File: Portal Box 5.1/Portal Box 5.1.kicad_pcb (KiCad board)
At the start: 2 copper layers, 120 x 80 mm, 79 parts, among them J1 USB_A, J2 USB_C, J3 A 14-LC-TT, J4 6871XX149022_687118149022, J5 RFID-RC522, J6 Conn_01x04, K1 PR28-5V-360-1A-E, Q1 NTR5103NT1G, Q2 NTR5103NT1G, SW1 BUTTON, SW2 SW_DPST, U1 USBLC6-2P6, U2 USBLC6-2P6, U3 TLE4971-A050T5-U-E0001, U4 AP7363-33D-13, U5 ESP32-S3-DEVKITC-1-N8R8-OFFIC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

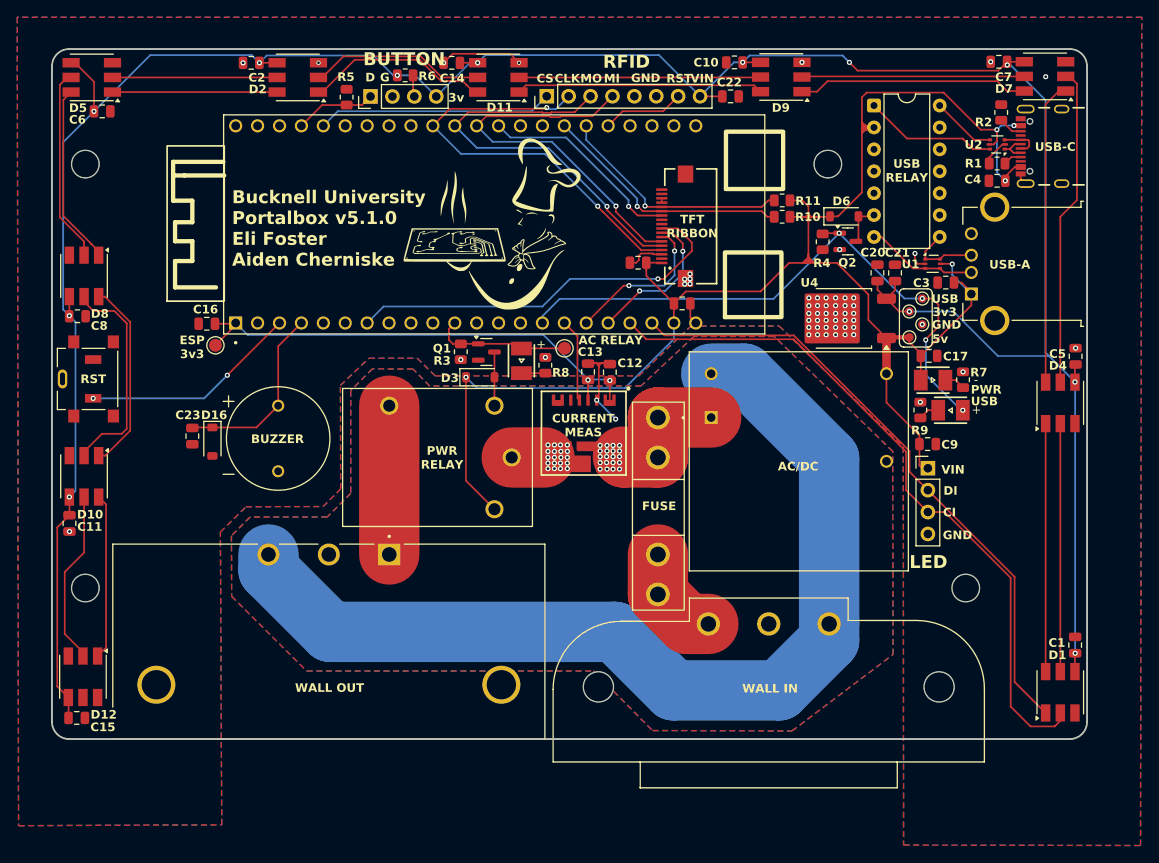
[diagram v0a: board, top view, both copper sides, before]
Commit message: update track clearances, mfg files
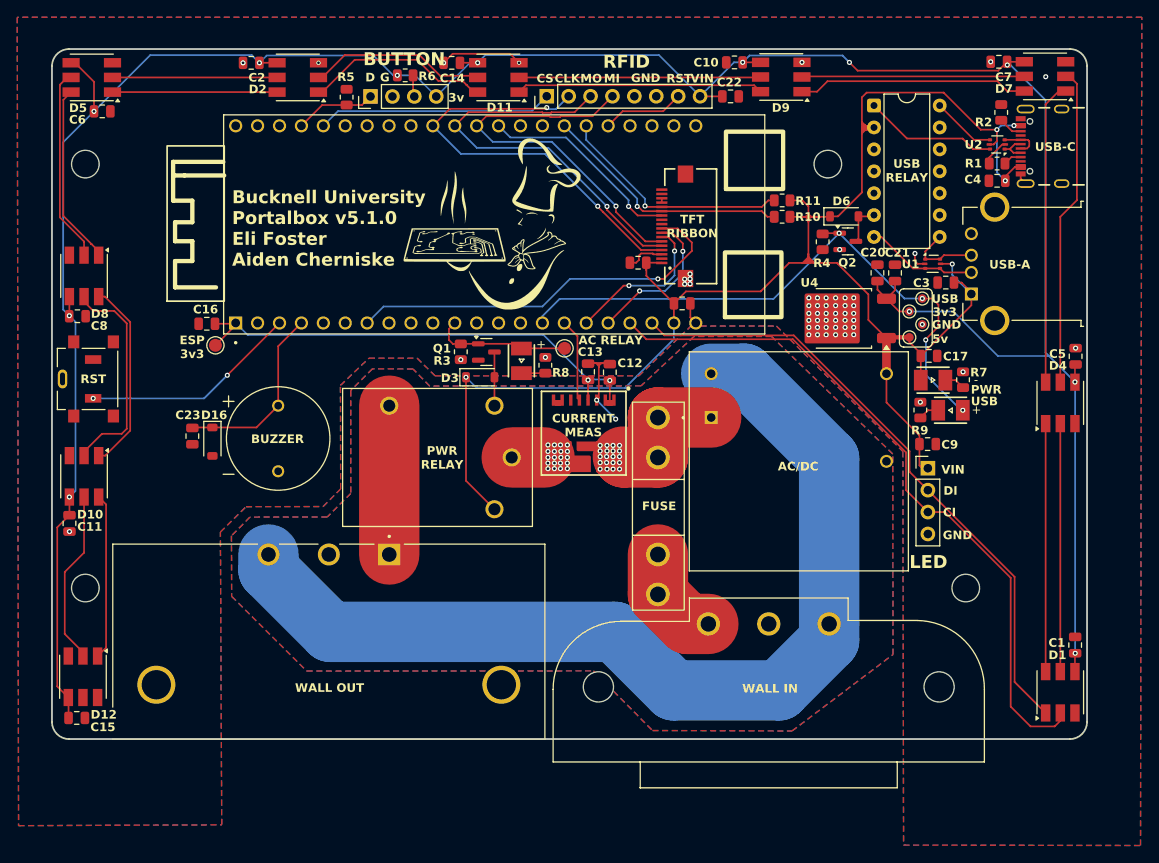
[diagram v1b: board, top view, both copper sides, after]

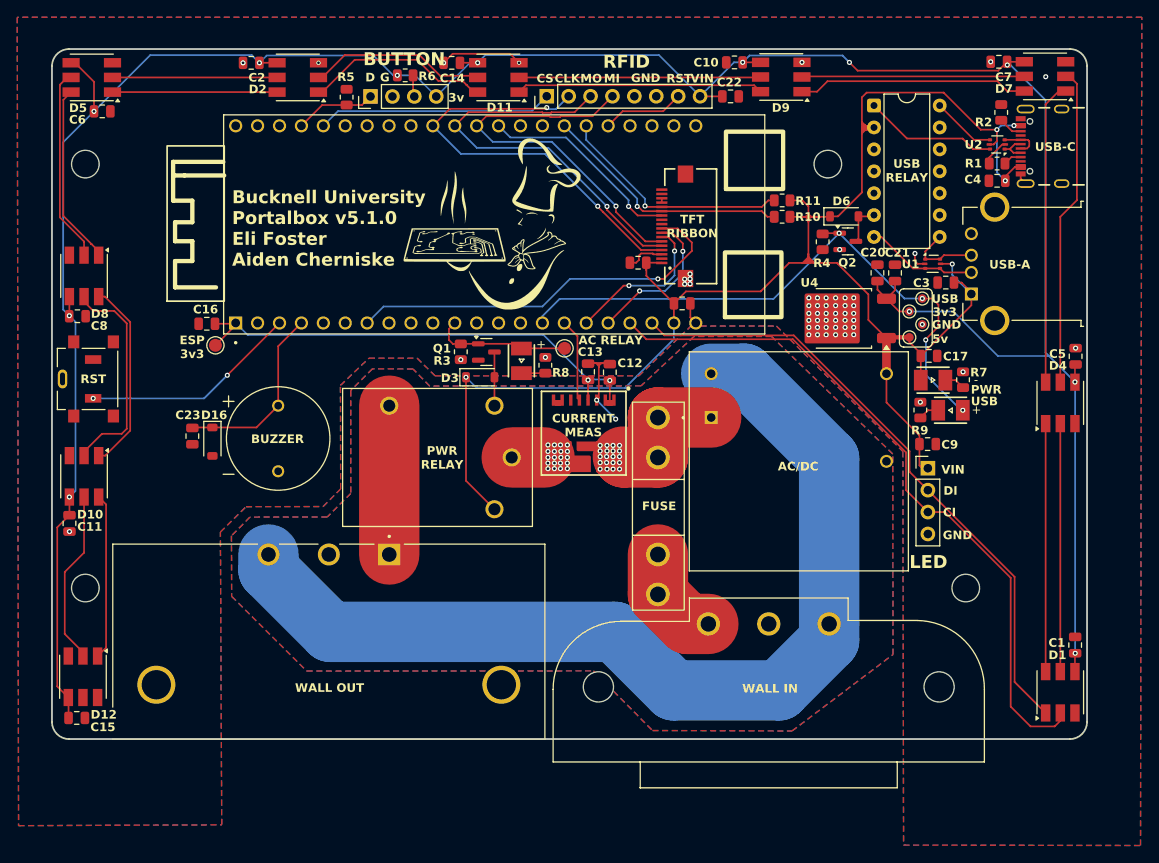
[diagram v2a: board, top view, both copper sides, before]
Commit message: change ac/dc and acm to dc ground, update planes
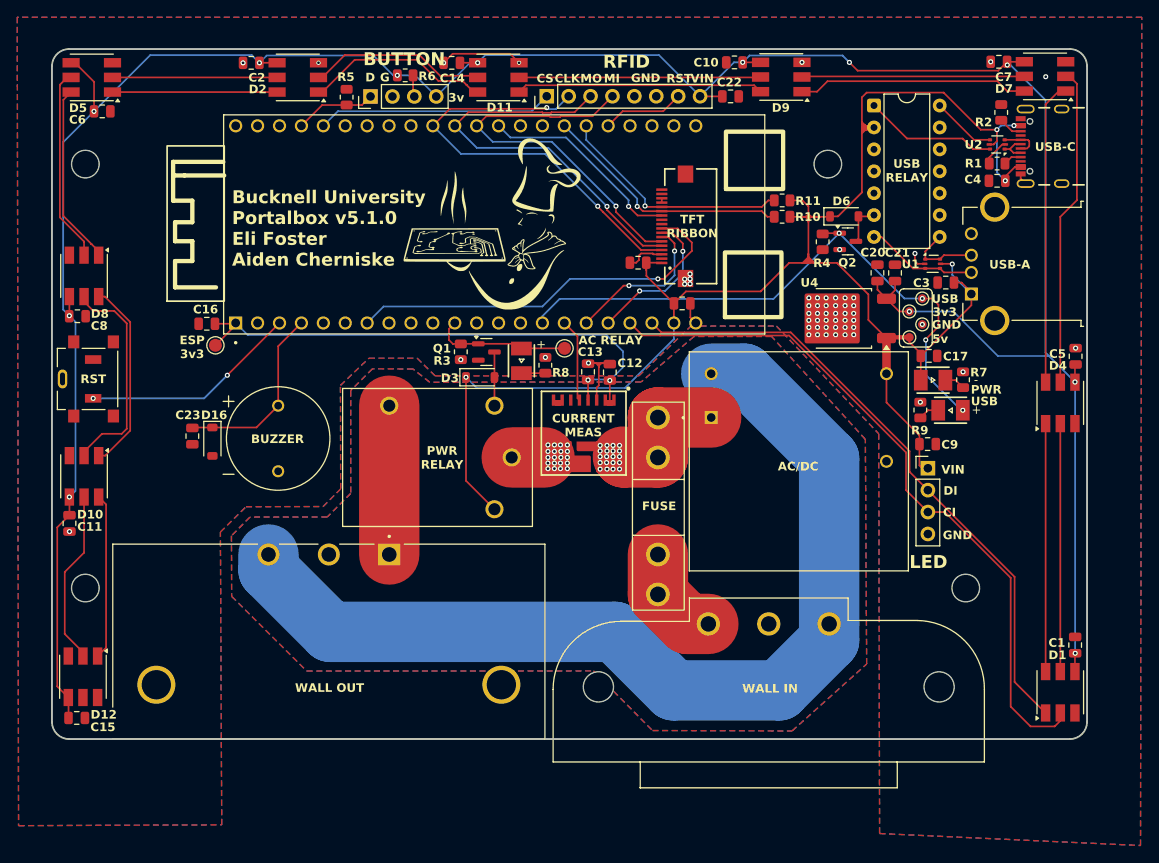
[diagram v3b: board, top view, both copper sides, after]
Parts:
- A1: value 703W-00_53 -> Q219-ND
- A2: value PX0675/PC -> 708-1351-ND
- BZ1: value Buzzer -> 668-AI-1223-TWT-5V-7-ND
- J1: value USB_A -> 609-87520-0010ALFCT-ND
- J2: value USB_C -> 2073-USB4105-GF-ACT-ND
- J4: value 6871XX149022_687118149022 -> 732-6001-1-ND
- PS1: value RACM06E-05SK_277 -> 945-RACM06E-05SK/277-ND
- SW1: value BUTTON -> 141-TL3336AF160QCT-ND
- U1, U2: value USBLC6-2P6 -> 497-5026-1-ND
- U3: value TLE4971-A050T5-U-E0001 -> 448-TLE4971A050T5UE0001XUMA1CT-ND
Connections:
- C12 pad 2: Earth -> GND
- C13 pad 2: Earth -> GND
- PS1 pad 4: Earth -> GND
- U3 pad 2: Earth -> GND
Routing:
- net Earth: track 12.5 -> 0.00 mm, vias 2 -> 0
- net GND: track 23.8 -> 33.2 mm, vias 57 -> 58
- net ESP3vo: track 58.0 -> 64.7 mm

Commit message: fix ground plane bulges, schematic and layout change for TVS diodes
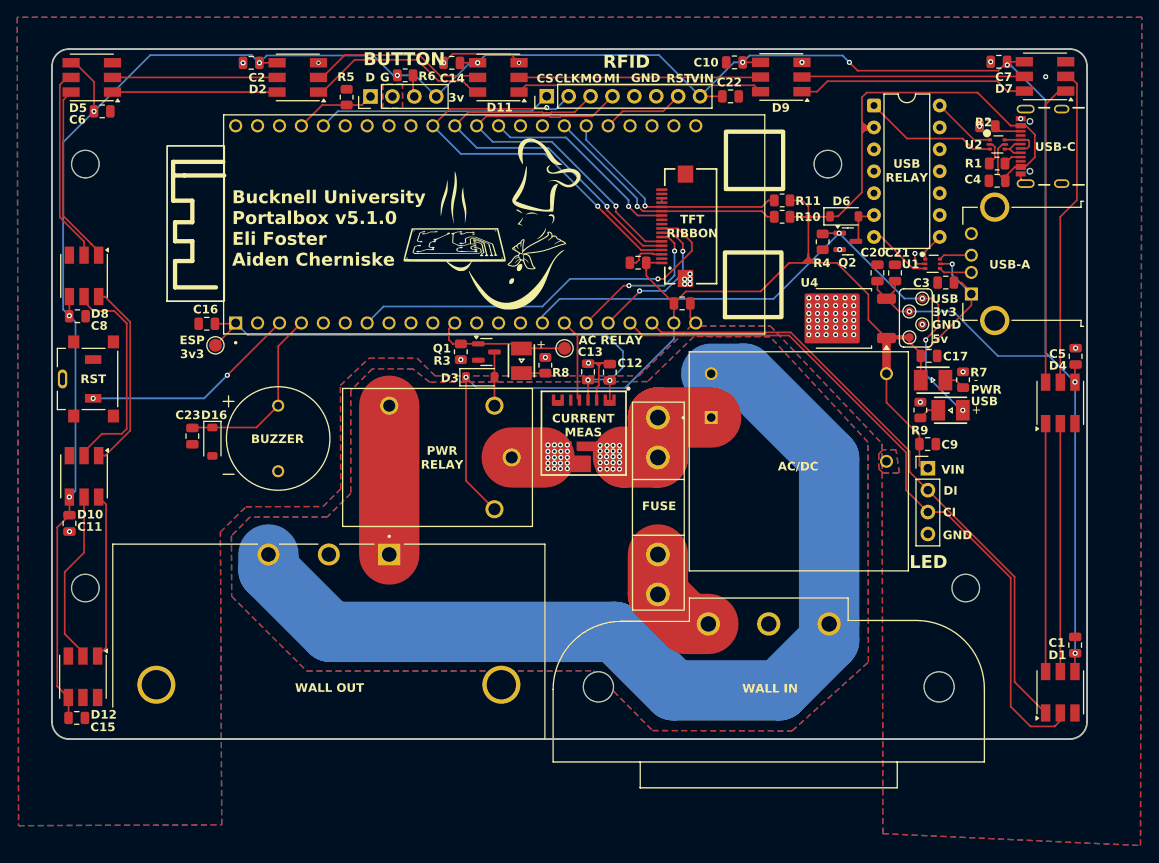
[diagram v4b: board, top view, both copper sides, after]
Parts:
- moved R2 2.26 mm to (197.4, 62.1), turned to 0 degrees
- turned U2 to 0 degrees
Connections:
- J1 pad 2: USBA_D- -> /A_D-
- J1 pad 3: USBA_D+ -> /A_D+
- U1 pad 4: USBA_D- -> /A_D-
- U1 pad 6: USBA_D+ -> /A_D+
- U2 pad 1: /C_D- -> USBC_D+
- U2 pad 3: /C_D+ -> USBC_D-
- U2 pad 4: USBC_D+ -> /C_D-
- U2 pad 6: USBC_D- -> /C_D+
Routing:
- net USBA_D+: track 8.84 -> 3.26 mm
- net USBA_D-: track 13.0 -> 7.46 mm
- net /A_D+: track 0.00 -> 3.87 mm
- net /A_D-: track 0.00 -> 3.83 mm
- net +5V: track 209.8 -> 212.7 mm, vias 5 -> 2
- net GND: track 33.2 -> 33.0 mm, vias 58 -> 60

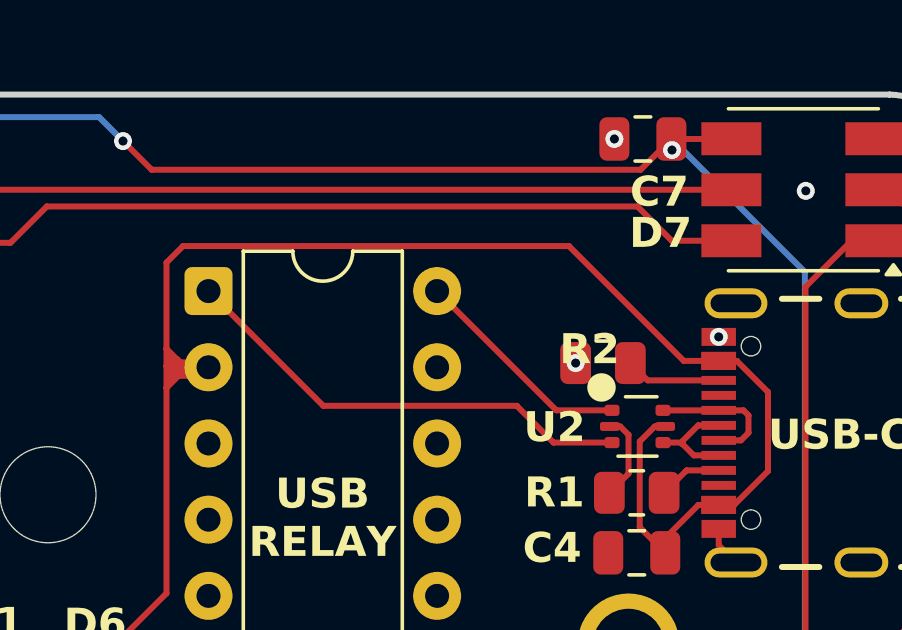
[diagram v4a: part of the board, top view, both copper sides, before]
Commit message: move r2 and fix silkscreening, update tvs diode footprint
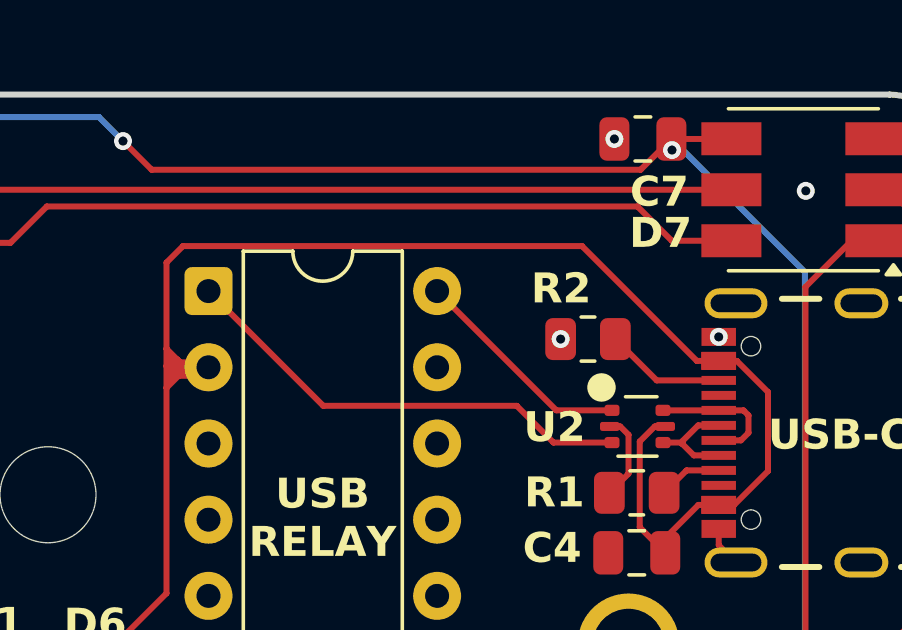
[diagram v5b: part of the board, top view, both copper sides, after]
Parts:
- moved R2 0.94 mm to (196.9, 61.3)
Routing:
- net /CC2: track 3.18 -> 4.02 mm
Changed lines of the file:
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@@
 	(footprint "Resistor_SMD:R_0805_2012Metric"
 		(layer "F.Cu")
-		(at 197.4 62.1)
+		(at 196.9 61.3)
 		(descr "Resistor SMD 0805 (2012 Metric), square (rectangular) end terminal, IPC-7351 nominal, (Body size source: IPC-SM-782 page 72, https://www.pcb-3d.com/wordpress/wp-content/uploads/ipc-sm-782a_amendment_1_and_2.pdf), generated with kicad-footprint-generator")
 		(tags "resistor")
@@
 	)
 	(gr_text "R2"
-		(at 195.95 62.225 0)
+		(at 195 60.2 0)
 		(layer "F.SilkS")
 		(effects
@@
 	)
 	(via
-		(at 196.4875 62.1)
+		(at 195.9875 61.3)
 		(size 0.6)
 		(drill 0.3)
@@
 	)
 	(segment
-		(start 196.265 58.2)
-		(end 183.4 58.2)
+		(start 200.5275 62.0275)
+		(end 196.7 58.2)
 		(width 0.2)
 		(layer "F.Cu")
@@
 	)
 	(segment
+		(start 182.85 58.75)
+		(end 182.85 61.625)
+		(width 0.2)
+		(layer "F.Cu")
+		(net 6)
+	)
+	(segment
 		(start 176.325 77.95)
 		(end 176.175 77.95)
@@
 	)
 	(segment
+		(start 183.4 58.2)
+		(end 182.85 58.75)
+		(width 0.2)
+		(layer "F.Cu")
+		(net 6)
+	)
+	(segment
 		(start 183.2 61.975)
 		(end 183.3 62.075)
@@
 	)
 	(segment
-		(start 183.4 58.2)
-		(end 182.85 58.75)
-		(width 0.2)
-		(layer "F.Cu")
-		(net 6)
-	)
-	(segment
 		(start 183.2 61.975)
 		(end 182.85 61.625)
@@
 	)
 	(segment
+		(start 201.2625 62.0275)
+		(end 200.5275 62.0275)
+		(width 0.2)
+		(layer "F.Cu")
+		(net 6)
+	)
+	(segment
 		(start 183.25 62.525)
 		(end 182.85 62.925)
@@
 	)
 	(segment
-		(start 201.2625 62.0275)
-		(end 200.0925 62.0275)
-		(width 0.2)
-		(layer "F.Cu")
-		(net 6)
-	)
-	(segment
 		(start 183.3 62.075)
 		(end 183.6 62.075)
@@
 	)
 	(segment
-		(start 182.85 58.75)
-		(end 182.85 61.625)
-		(width 0.2)
-		(layer "F.Cu")
-		(net 6)
-	)
-	(segment
 		(start 176.175 77.95)
 		(end 176.675 77.45)
@@
 	)
 	(segment
-		(start 200.0925 62.0275)
-		(end 196.265 58.2)
-		(width 0.2)
-		(layer "F.Cu")
-		(net 6)
-	)
-	(segment
 		(start 176.649 76.925)
 		(end 176.649 73.175)
@@
 	)
 	(segment
+		(start 196.7 58.2)
+		(end 183.4 58.2)
+		(width 0.2)
+		(layer "F.Cu")
+		(net 6)
+	)
+	(segment
 		(start 176.649 73.175)
 		(end 176.649 72.926)
@@
 	)
 	(segment
-		(start 198.89 62.6775)
-		(end 201.2575 62.6775)
+		(start 201.2575 62.6775)
+		(end 199.19 62.6775)
 		(width 0.2)
 		(layer "F.Cu")
@@
 	)
 	(segment
-		(start 198.3125 62.1)
-		(end 198.89 62.6775)
+		(start 199.19 62.6775)
+		(end 197.8125 61.3)
 		(width 0.2)
 		(layer "F.Cu")
@@
 	)
 	(zone
+		(net 6)
+		(net_name "+5V")
+		(layer "F.Cu")
+		(name "$teardrop_padvia$")
+		(hatch full 0.1)
+		(priority 30003)
+		(attr
+			(teardrop
+				(type padvia)
+			)
+		)
+		(connect_pads yes
+			(clearance 0)
+		)
+		(min_thickness 0.0254)
+		(filled_areas_thickness no)
+		(fill yes
+			(thermal_gap 0.5)
+			(thermal_bridge_width 0.5)
+			(island_removal_mode 1)
+			(island_area_min 10)
+		)
+		(polygon
+			(pts
+				(xy 185.1975 87.86) (xy 186.1975 87.86) (xy 186.298751 87.26) (xy 185.7 86.659) (xy 185.098747 87.26)
+			)
+		)
+	)
+	(zone
 		(net 0)
 		(net_name "")
@@
 	)
 	(zone
-		(net 4)
-		(net_name "+3V3")
+		(net 6)
+		(net_name "+5V")
 		(layer "F.Cu")
 		(name "$teardrop_padvia$")
 		(hatch full 0.1)
-		(priority 30004)
+		(priority 30006)
 		(attr
 			(teardrop
@@
 		(polygon
 			(pts
-				(xy 184.746447 81.005026) (xy 184.605026 81.146447) (xy 184.6 81.75) (xy 185.700707 82.100707) (xy 185.948528 81.5)
+				(xy 184.746447 85.565026) (xy 184.605026 85.706447) (xy 184.6 86.31) (xy 185.700707 86.660707) (xy 185.948528 86.06)
 			)
 		)
 	)
 	(zone
-		(net 6)
-		(net_name "+5V")
+		(net 4)
+		(net_name "+3V3")
 		(layer "F.Cu")
 		(name "$teardrop_padvia$")
 		(hatch full 0.1)
-		(priority 30003)
+		(priority 30005)
 		(attr
 			(teardrop
@@
 		(polygon
 			(pts
-				(xy 185.1975 87.86) (xy 186.1975 87.86) (xy 186.298751 87.26) (xy 185.7 86.659) (xy 185.098747 87.26)
+				(xy 186.653553 83.194974) (xy 186.794974 83.053553) (xy 186.8 82.45) (xy 185.699293 82.099293) (xy 185.451472 82.7)
 			)
 		)
@@
 		(name "$teardrop_padvia$")
 		(hatch full 0.1)
-		(priority 30008)
+		(priority 30009)
 		(attr
 			(teardrop
@@
 		(polygon
 			(pts
-				(xy 187.755764 83.475) (xy 187.755764 83.675) (xy 188.291473 83.869236) (xy 188.351 83.575) (xy 188.291473 83.280764)
+				(xy 207.65 91.155764) (xy 207.45 91.155764) (xy 207.255764 91.691473) (xy 207.55 91.751) (xy 207.844236 91.691473)
 			)
 		)
@@
 		(name "$teardrop_padvia$")
 		(hatch full 0.1)
-		(priority 30006)
+		(priority 30001)
 		(attr
 			(teardrop
@@
 		(polygon
 			(pts
-				(xy 184.746447 85.565026) (xy 184.605026 85.706447) (xy 184.6 86.31) (xy 185.700707 86.660707) (xy 185.948528 86.06)
+				(xy 187.4 86.825) (xy 187.4 86.325) (xy 186.645671 86.07903) (xy 185.699 86.66) (xy 186.690198 87.211217)
 			)
 		)
 	)
 	(zone
-		(net 4)
-		(net_name "+3V3")
+		(net 6)
+		(net_name "+5V")
 		(layer "F.Cu")
 		(name "$teardrop_padvia$")
 		(hatch full 0.1)
-		(priority 30005)
+		(priority 30000)
 		(attr
 			(teardrop
@@
 		(polygon
 			(pts
-				(xy 186.653553 83.194974) (xy 186.794974 83.053553) (xy 186.8 82.45) (xy 185.699293 82.099293) (xy 185.451472 82.7)
+				(xy 186.1975 89.296488) (xy 185.1975 89.296488) (xy 184.957988 90.642902) (xy 185.6975 90.791) (xy 186.437012 90.642902)
 			)
 		)
 	)
 	(zone
-		(net 6)
-		(net_name "+5V")
+		(net 4)
+		(net_name "+3V3")
 		(layer "F.Cu")
 		(name "$teardrop_padvia$")
 		(hatch full 0.1)
-		(priority 30001)
+		(priority 30008)
 		(attr
 			(teardrop
@@
 		(polygon
 			(pts
-				(xy 187.4 86.825) (xy 187.4 86.325) (xy 186.645671 86.07903) (xy 185.699 86.66) (xy 186.690198 87.211217)
+				(xy 187.755764 83.475) (xy 187.755764 83.675) (xy 188.291473 83.869236) (xy 188.351 83.575) (xy 188.291473 83.280764)
 			)
 		)
@@
 		(name "$teardrop_padvia$")
 		(hatch full 0.1)
-		(priority 30009)
+		(priority 30007)
 		(attr
 			(teardrop
@@
 		(polygon
 			(pts
-				(xy 207.65 91.155764) (xy 207.45 91.155764) (xy 207.255764 91.691473) (xy 207.55 91.751) (xy 207.844236 91.691473)
+				(xy 186.79 81.061543) (xy 186.59 81.061543) (xy 185.443817 81.5) (xy 185.7 82.101) (xy 186.8 81.75)
 			)
 		)
 	)
 	(zone
-		(net 6)
-		(net_name "+5V")
+		(net 4)
+		(net_name "+3V3")
 		(layer "F.Cu")
 		(name "$teardrop_padvia$")
 		(hatch full 0.1)
-		(priority 30000)
+		(priority 30004)
 		(attr
 			(teardrop
@@
 		(polygon
 			(pts
-				(xy 186.1975 89.296488) (xy 185.1975 89.296488) (xy 184.957988 90.642902) (xy 185.6975 90.791) (xy 186.437012 90.642902)
+				(xy 184.746447 81.005026) (xy 184.605026 81.146447) (xy 184.6 81.75) (xy 185.700707 82.100707) (xy 185.948528 81.5)
 			)
 		)
@@
 	)
 	(zone
-		(net 4)
-		(net_name "+3V3")
-		(layer "F.Cu")
-		(name "$teardrop_padvia$")
-		(hatch full 0.1)
-		(priority 30007)
-		(attr
-			(teardrop
-				(type padvia)
-			)
-		)
-		(connect_pads yes
-			(clearance 0)
-		)
-		(min_thickness 0.0254)
-		(filled_areas_thickness no)
-		(fill yes
-			(thermal_gap 0.5)
-			(thermal_bridge_width 0.5)
-			(island_removal_mode 1)
-			(island_area_min 10)
-		)
-		(polygon
-			(pts
-				(xy 186.79 81.061543) (xy 186.59 81.061543) (xy 185.443817 81.5) (xy 185.7 82.101) (xy 186.8 81.75)
-			)
-		)
-	)
-	(zone
 		(net 5)
 		(net_name "GND")
@@
 		(name "$teardrop_padvia$")
 		(hatch full 0.1)
-		(priority 30001)
+		(priority 30000)
 		(attr
 			(teardrop
@@
 		(polygon
 			(pts
-				(xy 188.944236 83.675) (xy 188.944236 83.475) (xy 188.408527 83.280764) (xy 188.349 83.575) (xy 188.408527 83.869236)
+				(xy 207.475 92.344236) (xy 207.675 92.344236) (xy 207.844236 91.808527) (xy 207.55 91.749) (xy 207.255764 91.808527)
 			)
 		)
@@
 		(name "$teardrop_padvia$")
 		(hatch full 0.1)
-		(priority 30000)
+		(priority 30001)
 		(attr
 			(teardrop
@@
 		(polygon
 			(pts
-				(xy 207.475 92.344236) (xy 207.675 92.344236) (xy 207.844236 91.808527) (xy 207.55 91.749) (xy 207.255764 91.808527)
+				(xy 188.944236 83.675) (xy 188.944236 83.475) (xy 188.408527 83.280764) (xy 188.349 83.575) (xy 188.408527 83.869236)
 			)
 		)

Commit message: update revision number :)
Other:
- board text added: "Bucknell University Portalbox v5.1.1 Eli Foster Aiden Cherniske"
- board text removed: "Bucknell University Portalbox v5.1.0 Eli Foster Aiden Cherniske"
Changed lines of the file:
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@@
 		)
 	)
-	(gr_text "Bucknell University\nPortalbox v5.1.0\nEli Foster\nAiden Cherniske"
+	(gr_text "Bucknell University\nPortalbox v5.1.1\nEli Foster\nAiden Cherniske"
 		(at 109.825 78.45 0)
 		(layer "F.SilkS")
